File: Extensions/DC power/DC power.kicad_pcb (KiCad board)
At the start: 2 copper layers, 29.9 x 14.5 mm, 7 parts, among them P1 Solder_Pad, P2 Solder_Pad, P3 Solder_Pad, SW1 TS-1102S-C-A-B, SW2 TS-1102S-C-A-B

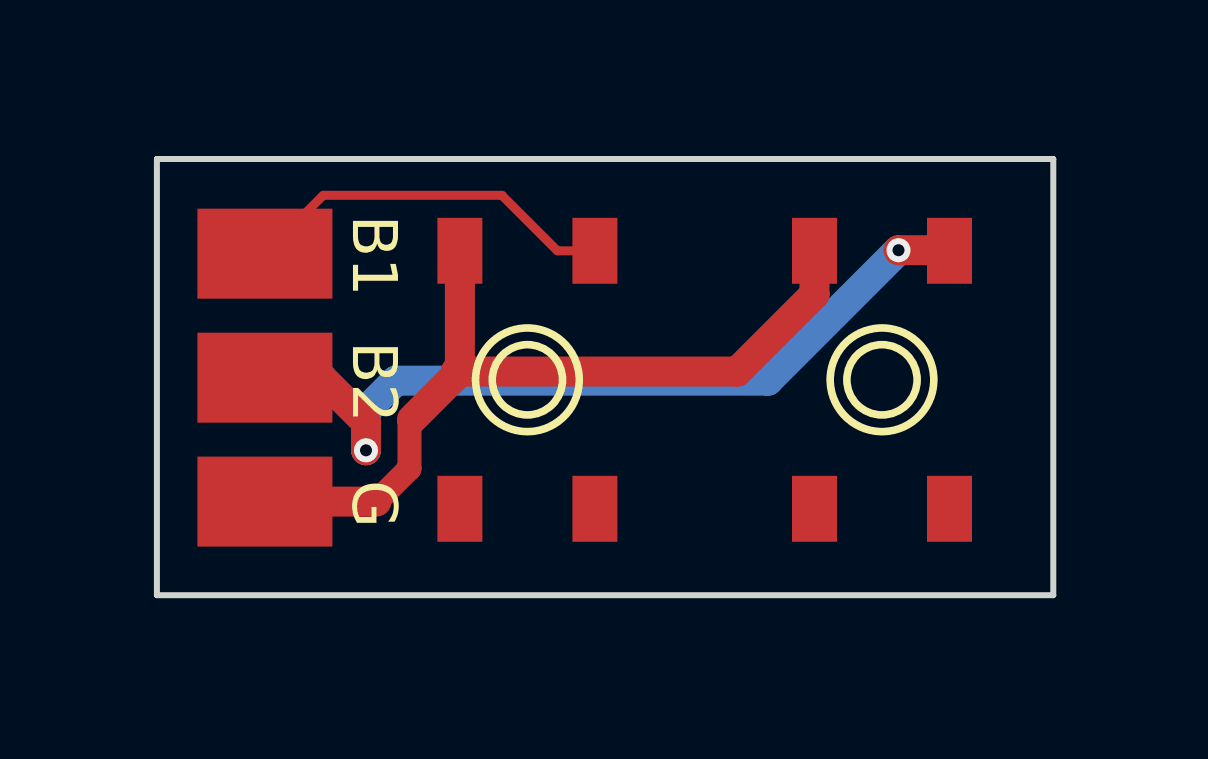
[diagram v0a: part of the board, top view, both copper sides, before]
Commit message: updated button extension, added DC power extension
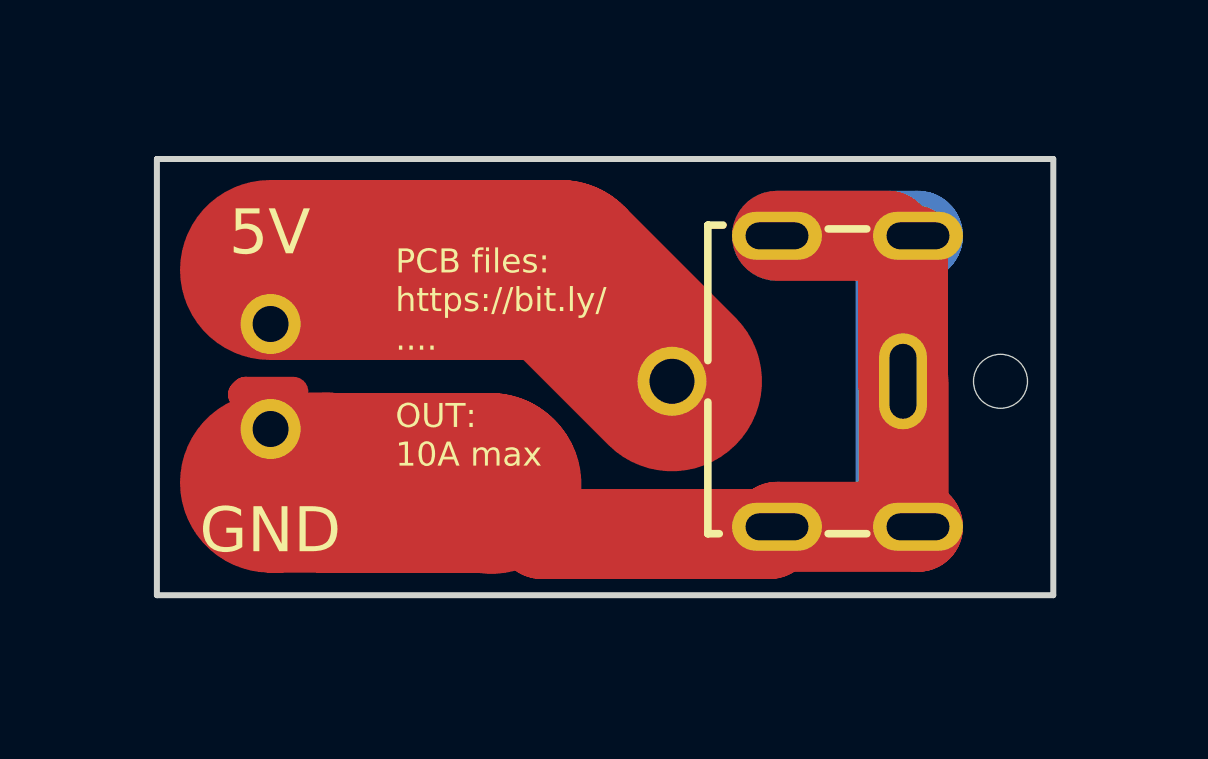
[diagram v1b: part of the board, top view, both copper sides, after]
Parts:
- removed G***: LOGO, LOGO
- removed P1, P2, P3: Solder_Pad, footprint:Solder pad
- removed SW1, SW2: TS-1102S-C-A-B, footprint:KEY-SMD_4P-L6.0-W6.0-P4.50-LS8.6
- added PWR1: DC-042C-Z-2_5-A, footprint:DC-IN-TH_DC-042C-Z-2.5-A, F.Cu at (149.8, 101.7)
- added U1: KF350-3_5-2P, footprint:CONN-TH_P3.50_KF350-3.5-2P, F.Cu at (129.7, 101.6)
- moved designedby 9.40 mm to (138.0, 105.6), turned to 0 degrees
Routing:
- net GND: track 27.7 -> 57.6 mm
- net BUTTON2: track 27.9 -> 0.00 mm, vias 2 -> 0
- net +5V: track 0.00 -> 14.9 mm
- net BUTTON1: track 12.6 -> 0.00 mm
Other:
- board text added: "5V"
- board text added: "DC PCB v1.0 RC1"
- board text added: "GND"
- board text added: "PCB files: https://bit.ly/ .... OUT: 10A max"
- board text removed: "B1"
- board text removed: "B2"
- board text removed: "Buttons PCB v1.0 RC1"
- board text removed: "G"
- board text removed: "PCB files: https://bit.ly/ 3Idt9md"

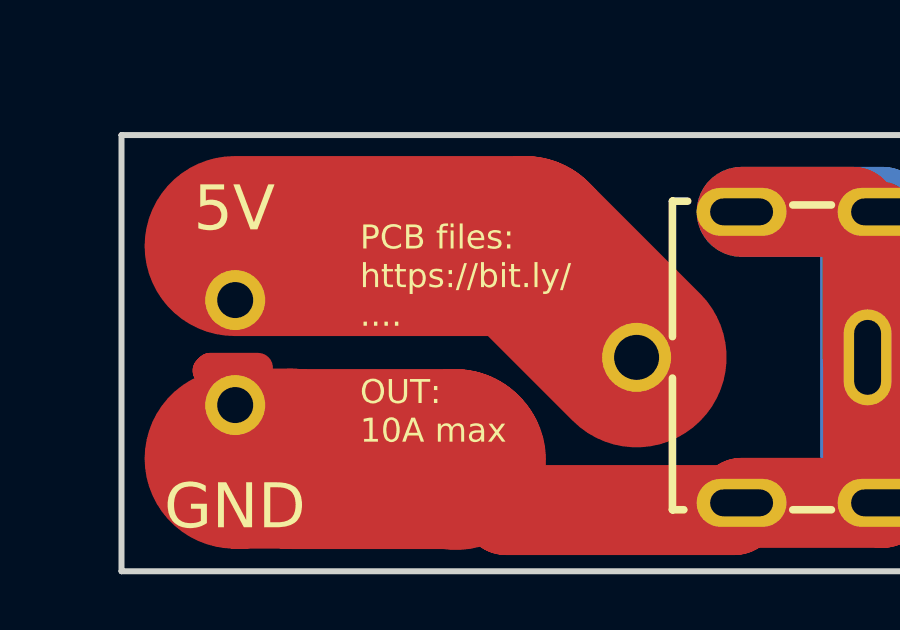
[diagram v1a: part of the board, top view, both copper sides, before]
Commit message: updated link on pcb
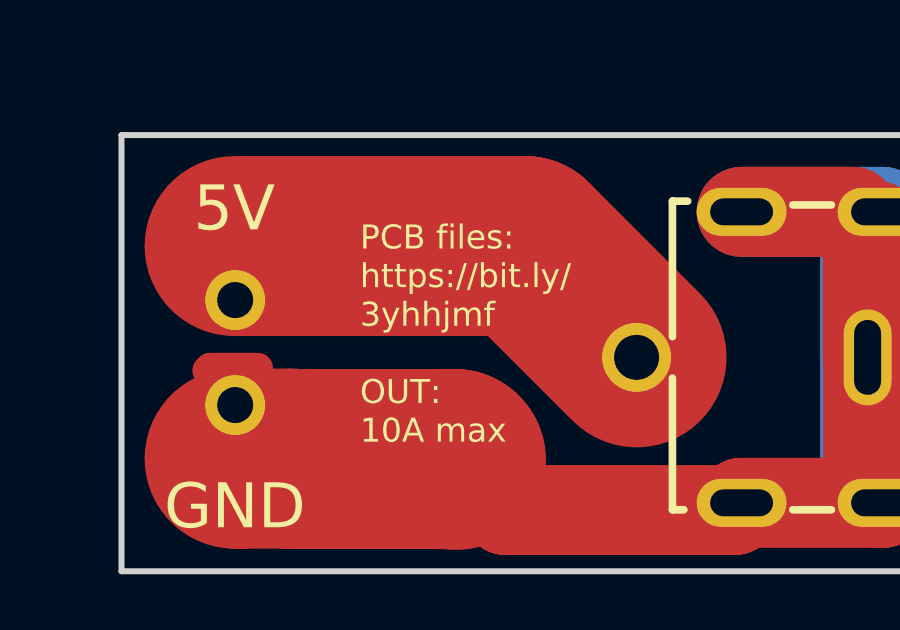
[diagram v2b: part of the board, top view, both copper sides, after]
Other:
- board text added: "PCB files: https://bit.ly/ 3yhhjmf OUT: 10A max"
- board text removed: "PCB files: https://bit.ly/ .... OUT: 10A max"
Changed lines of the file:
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@@
     (effects (font (size 1.5 1.5) (thickness 0.2)))
   )
-  (gr_text "PCB files:\nhttps://bit.ly/\n....\n\nOUT:\n10A max" (at 133.84 100.96) (layer "F.SilkS")
+  (gr_text "PCB files:\nhttps://bit.ly/\n3yhhjmf\n\nOUT:\n10A max" (at 133.84 100.96) (layer "F.SilkS")
     (effects (font (size 0.8 0.8) (thickness 0.15)) (justify left))
   )
